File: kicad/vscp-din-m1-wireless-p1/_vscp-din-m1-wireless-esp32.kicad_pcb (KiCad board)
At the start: 2 copper layers, 64.8 x 51 mm, 31 parts, among them J1 Conn_01x04_Left, J2 Conn_01x04_Right, J3 Conn_01x06, Q1 BC547, U1 ESP32-WROOM-32D, U2 ESP-12E

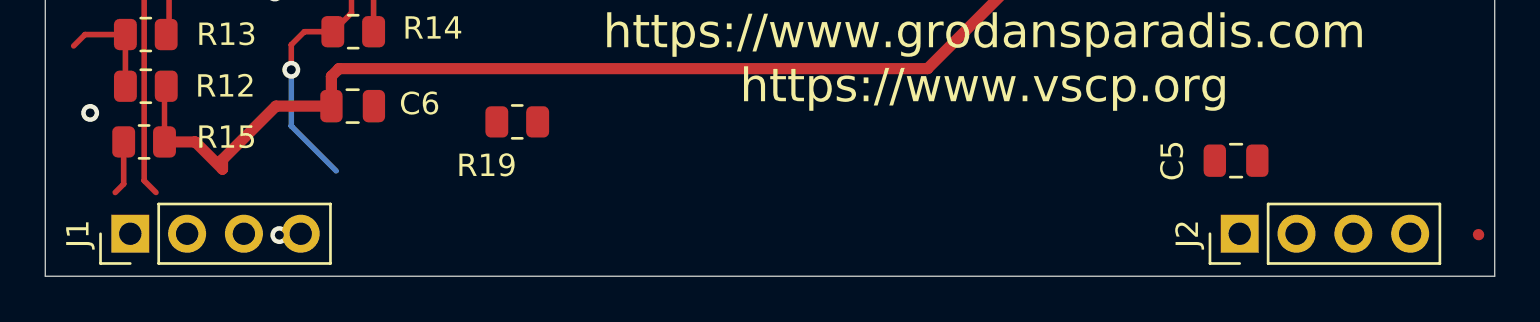
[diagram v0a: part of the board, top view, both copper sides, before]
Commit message: Added vanilla DIN board
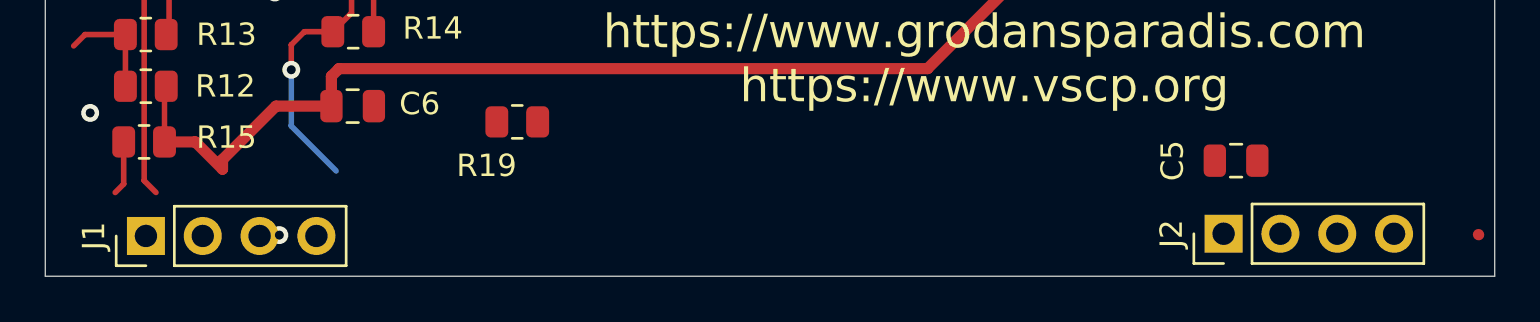
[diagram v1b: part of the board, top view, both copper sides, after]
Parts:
- moved J2 0.72 mm to (157.9, 119.8)
- moved J1 0.71 mm to (109.7, 119.9)
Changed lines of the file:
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@@
   )
   (module Connector_PinHeader_2.54mm:PinHeader_1x04_P2.54mm_Vertical (layer F.Cu)
-    (at 158.6 119.8 90)
+    (at 157.88 119.8 90)
     (descr "Through hole straight pin header, 1x04, 2.54mm pitch, single row")
     (tags "Through hole pin header THT 1x04 2.54mm single row")
@@
   )
   (module Connector_PinHeader_2.54mm:PinHeader_1x04_P2.54mm_Vertical (layer F.Cu)
-    (at 109 119.8 90)
+    (at 109.7 119.9 90)
     (descr "Through hole straight pin header, 1x04, 2.54mm pitch, single row")
     (tags "Through hole pin header THT 1x04 2.54mm single row")
@@
     )
   )
-  (dimension 2 (width 0.15) (layer Dwgs.User)
-    (gr_text "2,000 mm" (at 169 125.9) (layer Dwgs.User)
+  (dimension 48.18 (width 0.15) (layer Dwgs.User)
+    (gr_text "48,180 mm" (at 133.79 124) (layer Dwgs.User)
       (effects (font (size 1 1) (thickness 0.15)))
     )
-    (feature1 (pts (xy 168 121.3) (xy 168 125.186421)))
-    (feature2 (pts (xy 170 121.3) (xy 170 125.186421)))
-    (crossbar (pts (xy 170 124.6) (xy 168 124.6)))
-    (arrow1a (pts (xy 168 124.6) (xy 169.126504 124.013579)))
-    (arrow1b (pts (xy 168 124.6) (xy 169.126504 125.186421)))
-    (arrow2a (pts (xy 170 124.6) (xy 168.873496 124.013579)))
-    (arrow2b (pts (xy 170 124.6) (xy 168.873496 125.186421)))
+    (feature1 (pts (xy 109.7 119.8) (xy 109.7 123.286421)))
+    (feature2 (pts (xy 157.88 119.8) (xy 157.88 123.286421)))
+    (crossbar (pts (xy 157.88 122.7) (xy 109.7 122.7)))
+    (arrow1a (pts (xy 109.7 122.7) (xy 110.826504 122.113579)))
+    (arrow1b (pts (xy 109.7 122.7) (xy 110.826504 123.286421)))
+    (arrow2a (pts (xy 157.88 122.7) (xy 156.753496 122.113579)))
+    (arrow2b (pts (xy 157.88 122.7) (xy 156.753496 123.286421)))
   )
-  (dimension 2 (width 0.15) (layer Dwgs.User)
-    (gr_text "2,000 mm" (at 106.2 125.2) (layer Dwgs.User)
+  (dimension 2.7 (width 0.15) (layer Dwgs.User)
+    (gr_text "2,700 mm" (at 106.55 124.4) (layer Dwgs.User)
       (effects (font (size 1 1) (thickness 0.15)))
     )
-    (feature1 (pts (xy 107.2 121.3) (xy 107.2 124.486421)))
-    (feature2 (pts (xy 105.2 121.3) (xy 105.2 124.486421)))
-    (crossbar (pts (xy 105.2 123.9) (xy 107.2 123.9)))
-    (arrow1a (pts (xy 107.2 123.9) (xy 106.073496 124.486421)))
-    (arrow1b (pts (xy 107.2 123.9) (xy 106.073496 123.313579)))
-    (arrow2a (pts (xy 105.2 123.9) (xy 106.326504 124.486421)))
-    (arrow2b (pts (xy 105.2 123.9) (xy 106.326504 123.313579)))
+    (feature1 (pts (xy 107.9 121.5) (xy 107.9 123.686421)))
+    (feature2 (pts (xy 105.2 121.5) (xy 105.2 123.686421)))
+    (crossbar (pts (xy 105.2 123.1) (xy 107.9 123.1)))
+    (arrow1a (pts (xy 107.9 123.1) (xy 106.773496 123.686421)))
+    (arrow1b (pts (xy 107.9 123.1) (xy 106.773496 122.513579)))
+    (arrow2a (pts (xy 105.2 123.1) (xy 106.326504 123.686421)))
+    (arrow2b (pts (xy 105.2 123.1) (xy 106.326504 122.513579)))
   )
   (gr_line (start 105.2 86.7) (end 105.2 121.7) (layer Edge.Cuts) (width 0.05))
@@
   (segment (start 108.7825 110.8965) (end 108.7806 110.8946) (width 0.25) (layer F.Cu) (net 2))
   (segment (start 108.7825 113.206) (end 108.7825 110.8965) (width 0.25) (layer F.Cu) (net 2))
-  (via (at 115.664 119.8608) (size 0.8) (drill 0.4) (layers F.Cu B.Cu) (net 39))
   (segment (start 106.9772 110.8946) (end 106.4692 111.4026) (width 0.25) (layer F.Cu) (net 2))
   (segment (start 108.7806 110.8946) (end 106.9772 110.8946) (width 0.25) (layer F.Cu) (net 2))
@@
   (segment (start 167.9353 88.2867) (end 167.9588 88.2632) (width 0.25) (layer F.Cu) (net 5))
   (segment (start 167.9353 91.7938) (end 167.9353 88.2867) (width 0.25) (layer F.Cu) (net 5))
+  (via (at 115.664 119.8608) (size 0.8) (drill 0.4) (layers F.Cu B.Cu) (net 39))
   (via (at 150.4112 79.8558) (size 0.8) (drill 0.4) (layers F.Cu B.Cu) (net 39))
   (via (at 143.4516 104.6716) (size 0.8) (drill 0.4) (layers F.Cu B.Cu) (net 39))
